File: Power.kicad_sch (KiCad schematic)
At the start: 43 parts, among them J10 Conn_01x02_Socket, J22 Conn_01x02_Socket, J23 Conn_01x02_Socket, J9 Barrel_Jack, Q1 NMOS, U10 INA219AxD, U11 TLV62569ADRL, U15 TPS60400DBV, U9 INA219AxD

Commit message: Schematic tiddy up
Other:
- title: (none) -> Power Schematic
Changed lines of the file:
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@@
 	(generator_version "10.0")
 	(paper "A4")
+	(title_block
+		(title "Power Schematic")
+		(date "2026-10-17")
+		(rev "0")
+		(comment 1 "Javier Aldana + Xander Beal")
+	)
 	(rectangle
 		(start 110.49 101.6)

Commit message: small changes
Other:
- moved on the sheet: C43, C47, C48, C49, C50, D4, J22, J23, R33, R38, R39, U15

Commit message: Final PCB from Xander
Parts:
- removed J9: Barrel_Jack, Connector_BarrelJack:BarrelJack_SwitchcraftConxall_RAPC10U_Horizontal, symbol Connector:Barrel_Jack
- added J24: Conn_01x02_Socket, Connector_Phoenix_SPT:PhoenixContact_SPT_2.5_2-H-5.0_1x02_P5.0mm_Horizontal, symbol Connector:Conn_01x02_Socket
- F1: footprint Resistor_THT:R_Axial_DIN0204_L3.6mm_D1.6mm_P5.08mm_Horizontal -> Fuse:Fuseholder_Clip-5x20mm_Keystone_3512P_Inline_P23.62x7.27mm_D1.02x2.41x1.02x1.57mm_Horizontal
- J22, J23: footprint Connector_PinSocket_2.54mm:PinSocket_1x02_P2.54mm_Vertical -> Connector_PinHeader_2.54mm:PinHeader_1x02_P2.54mm_Vertical
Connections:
- net 5V: now also J10.2 (Pin_2); no longer J10.1 (Pin_1)
- net GND: now also J24.1 (Pin_1)
- net at Q1.2 (D): now also J10.1 (Pin_1); no longer J10.2 (Pin_2)
- net at F1.1: now also J24.2 (Pin_2)
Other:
- moved on the sheet: J10

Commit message: second buck
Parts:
- added C1: 1u, Capacitor_SMD:C_0603_1608Metric, symbol Device:C
- added C2, C4: 100n, symbol Device:C
- added C3: 66u, symbol Device:C
- added C5: 470pF, symbol Device:C
- added C6: 22u, Capacitor_SMD:C_0805_2012Metric, symbol Device:C
- added L2: 1.5u, symbol Device:L
- added R1: 100k, Resistor_SMD:R_0603_1608Metric, symbol Device:R
- added R2: 1k, symbol Device:R
- added R3: 73.2k, Resistor_SMD:R_0402_1005Metric, symbol Device:R
- added R4: 10k, Resistor_SMD:R_0402_1005Metric, symbol Device:R
- added U2: TPS513885VABR, VAB0013A-MFG, symbol TPS51388:TPS513885VABR
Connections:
- net GND: now also C1.2, C2.2, C3.2, C6.2, R4.2, U2.11 (PGND), U2.3 (PGND), U2.9 (FBG)
- new net: R2.1, R3.2, R4.1, U2.7 (FB)
- new net: C4.2, L2.1
- new net: C1.1, R1.1, U2.10 (VCC), U2.5 (MODE)
- new net: R1.2, U2.4 (PG)
- new net: C4.1, U2.12 (SW), U2.13 (VBST), U2.2 (SW)
- new net: C5.1, R2.2
- new net +12V: C2.1, C3.1, U2.1 (VIN)
- new net +3V3: U2.6 (EN)
- new net +5V: C5.2, C6.1, L2.2, R3.1

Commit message: bucks
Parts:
- added C7, C8: 22, symbol Device:C
- C2, C4: footprint (none) -> Capacitor_SMD:C_0603_1608Metric
- C3: value 66u -> 22
- C5: footprint (none) -> Capacitor_SMD:C_0402_1005Metric
- L2: footprint (none) -> Inductor_SMD:IHLP5050EZER1R5M01
- R2: footprint (none) -> Resistor_SMD:R_0603_1608Metric
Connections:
- net GND: no longer C3.2
- net +12V renamed 20
- net 20: no longer C3.1
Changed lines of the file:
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@@
 			)
 		)
-		(property "Footprint" ""
+		(property "Footprint" "Capacitor_SMD:C_0603_1608Metric"
 			(at 157.1752 205.74 0)
 			(hide yes)
@@
 			)
 		)
-		(property "Value" "+12V"
+		(property "Value" "20"
 			(at 146.05 173.99 0)
 			(show_name no)
@@
 			)
 		)
-		(property "Footprint" ""
+		(property "Footprint" "Inductor_SMD:IHLP5050EZER1R5M01"
 			(at 260.35 173.99 0)
 			(hide yes)
@@
 			)
 		)
-		(property "Description" "Inductor"
+		(property "Description" "IHLP5050EZER1R5M01"
 			(at 260.35 173.99 0)
 			(hide yes)
@@
 	)
 	(symbol
+		(lib_id "Device:C")
+		(at 134.62 200.66 0)
+		(unit 1)
+		(body_style 1)
+		(exclude_from_sim no)
+		(in_bom yes)
+		(on_board yes)
+		(in_pos_files yes)
+		(dnp no)
+		(fields_autoplaced yes)
+		(property "Reference" "C3"
+			(at 138.43 199.3899 0)
+			(show_name no)
+			(do_not_autoplace no)
+			(effects
+				(font
+					(size 1.27 1.27)
+				)
+				(justify left)
+			)
+		)
+		(property "Value" "22"
+			(at 138.43 201.9299 0)
+			(show_name no)
+			(do_not_autoplace no)
+			(effects
+				(font
+					(size 1.27 1.27)
+				)
+				(justify left)
+			)
+		)
+		(property "Footprint" ""
+			(at 135.5852 204.47 0)
+			(hide yes)
+			(show_name no)
+			(do_not_autoplace no)
+			(effects
+				(font
+					(size 1.27 1.27)
+				)
+			)
+		)
+		(property "Datasheet" ""
+			(at 134.62 200.66 0)
+			(hide yes)
+			(show_name no)
+			(do_not_autoplace no)
+			(effects
+				(font
+					(size 1.27 1.27)
+				)
+			)
+		)
+		(property "Description" "CL31A226KAHNNNE"
+			(at 134.62 200.66 0)
+			(hide yes)
+			(show_name no)
+			(do_not_autoplace no)
+			(effects
+				(font
+					(size 1.27 1.27)
+				)
+			)
+		)
+		(pin "2"
+		)
+		(pin "1"
+		)
+		(instances
+			(project "Power"
+				(path "/ce54564b-053f-4184-8bbf-14aa73263a86"
+					(reference "C3")
+					(unit 1)
+				)
+			)
+		)
+	)
+	(symbol
 		(lib_id "power:+3V3")
 		(at 41.91 111.76 0)
@@
 			)
 		)
-		(property "Footprint" ""
+		(property "Footprint" "Capacitor_SMD:C_0603_1608Metric"
 			(at 248.92 173.0248 0)
 			(hide yes)
@@
 			)
 		)
-		(property "Description" "Unpolarized capacitor"
+		(property "Description" "EMK107B7104KA-T"
 			(at 245.11 173.99 0)
 			(hide yes)
@@
 			)
 		)
-		(property "Footprint" ""
+		(property "Footprint" "Capacitor_SMD:C_0402_1005Metric"
 			(at 279.4 188.2648 0)
 			(hide yes)
@@
 			)
 		)
-		(property "Description" "Unpolarized capacitor"
+		(property "Description" "GRM1555C1E471JA01D"
 			(at 275.59 189.23 0)
 			(hide yes)
@@
 	(symbol
 		(lib_id "Device:C")
-		(at 146.05 201.93 0)
+		(at 124.46 200.66 0)
 		(unit 1)
 		(body_style 1)
@@
 		(dnp no)
 		(fields_autoplaced yes)
-		(property "Reference" "C3"
-			(at 149.86 200.6599 0)
+		(property "Reference" "C7"
+			(at 128.27 199.3899 0)
 			(show_name no)
 			(do_not_autoplace no)
@@
 			)
 		)
-		(property "Value" "66u"
-			(at 149.86 203.1999 0)
+		(property "Value" "22"
+			(at 128.27 201.9299 0)
 			(show_name no)
 			(do_not_autoplace no)
@@
 		)
 		(property "Footprint" ""
-			(at 147.0152 205.74 0)
+			(at 125.4252 204.47 0)
 			(hide yes)
 			(show_name no)
@@
 			)
 		)
-		(property "Datasheet" ""
-			(at 146.05 201.93 0)
+		(property "Datasheet" "CL31A226KAHNNNE"
+			(at 124.46 200.66 0)
 			(hide yes)
 			(show_name no)
@@
 			)
 		)
-		(property "Description" "Unpolarized capacitor"
-			(at 146.05 201.93 0)
+		(property "Description" "CL31A226KAHNNNE"
+			(at 124.46 200.66 0)
 			(hide yes)
 			(show_name no)
@@
 			)
 		)
-		(pin "1"
-		)
 		(pin "2"
 		)
+		(pin "1"
+		)
 		(instances
 			(project "Power"
 				(path "/ce54564b-053f-4184-8bbf-14aa73263a86"
-					(reference "C3")
+					(reference "C7")
 					(unit 1)
 				)
@@
 	)
 	(symbol
+		(lib_id "Device:C")
+		(at 114.3 200.66 0)
+		(unit 1)
+		(body_style 1)
+		(exclude_from_sim no)
+		(in_bom yes)
+		(on_board yes)
+		(in_pos_files yes)
+		(dnp no)
+		(fields_autoplaced yes)
+		(property "Reference" "C8"
+			(at 118.11 199.3899 0)
+			(show_name no)
+			(do_not_autoplace no)
+			(effects
+				(font
+					(size 1.27 1.27)
+				)
+				(justify left)
+			)
+		)
+		(property "Value" "22"
+			(at 118.11 201.9299 0)
+			(show_name no)
+			(do_not_autoplace no)
+			(effects
+				(font
+					(size 1.27 1.27)
+				)
+				(justify left)
+			)
+		)
+		(property "Footprint" ""
+			(at 115.2652 204.47 0)
+			(hide yes)
+			(show_name no)
+			(do_not_autoplace no)
+			(effects
+				(font
+					(size 1.27 1.27)
+				)
+			)
+		)
+		(property "Datasheet" ""
+			(at 114.3 200.66 0)
+			(hide yes)
+			(show_name no)
+			(do_not_autoplace no)
+			(effects
+				(font
+					(size 1.27 1.27)
+				)
+			)
+		)
+		(property "Description" "CL31A226KAHNNNE"
+			(at 114.3 200.66 0)
+			(hide yes)
+			(show_name no)
+			(do_not_autoplace no)
+			(effects
+				(font
+					(size 1.27 1.27)
+				)
+			)
+		)
+		(pin "2"
+		)
+		(pin "1"
+		)
+		(instances
+			(project "Power"
+				(path "/ce54564b-053f-4184-8bbf-14aa73263a86"
+					(reference "C8")
+					(unit 1)
+				)
+			)
+		)
+	)
+	(symbol
 		(lib_id "Connector:Conn_01x02_Socket")
 		(at 24.13 29.21 0)
@@
 			)
 		)
-		(property "Footprint" ""
+		(property "Footprint" "Resistor_SMD:R_0603_1608Metric"
 			(at 252.73 191.008 90)
 			(hide yes)
@@
 			)
 		)
-		(property "Description" "Resistor"
+		(property "Description" "EMK107B7104KA-T"
 			(at 252.73 189.23 0)
 			(hide yes)

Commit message: fixing some ERC issues
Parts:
- C3, C7, C8: footprint (none) -> Capacitor_SMD:C_1210_3225Metric
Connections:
- net 20: now also C3.1, C7.1, C8.1
- net GND: now also C3.2, C7.2, C8.2
- net at C4.2, L2.1: now also U2.12 (SW), U2.2 (SW)
- net at C4.1, U2.13 (VBST): no longer U2.12 (SW), U2.2 (SW)
- no-connect marks 0 -> 1
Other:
- moved on the sheet: C3, C7, C8

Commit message: footprintfor buck
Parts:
- removed C4: 100n, Capacitor_SMD:C_0603_1608Metric, symbol Device:C
- removed C5: 470pF, Capacitor_SMD:C_0402_1005Metric, symbol Device:C
- removed C6: 22u, Capacitor_SMD:C_0805_2012Metric, symbol Device:C
- removed R2: 1k, Resistor_SMD:R_0603_1608Metric, symbol Device:R
- removed R3: 73.2k, Resistor_SMD:R_0402_1005Metric, symbol Device:R
- removed U2: TPS513885VABR, VAB0013A-MFG, symbol TPS51388:TPS513885VABR
- added C30: 100n, Capacitor_SMD:C_0603_1608Metric, symbol Device:C
- added C31: 470pF, Capacitor_SMD:C_0402_1005Metric, symbol Device:C
- added C56: 22u, Capacitor_SMD:C_0805_2012Metric, symbol Device:C
- added J9: Conn_01x02_Pin, Connector_PinHeader_2.54mm:PinHeader_1x02_P2.54mm_Vertical, symbol Connector:Conn_01x02_Pin
- added R16: 1k, Resistor_SMD:R_0603_1608Metric, symbol Device:R
- added R63: 73.2k, Resistor_SMD:R_0402_1005Metric, symbol Device:R
- added U4: TPS513885VABR, TPS513885VABR:VAB0013A-MFG, symbol TPS51388:TPS513885VABR
- renumbered C8 to C61, C7 to C62, C3 to C63, C2 to C64, C1 to C65, L2 to L10
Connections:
- net +3V3: now also U4.6 (EN)
- net +5V: now also C31.2, C56.1, R63.1
- net GND: now also C56.2, J9.2 (Pin_2), U4.11 (PGND), U4.3 (PGND), U4.9 (FBG)
- net at R4.1: now also R16.1, R63.2, U4.7 (FB)
- net at L10.1: now also C30.2, U4.12 (SW), U4.2 (SW)
- net at C65.1, R1.1: now also U4.10 (VCC), U4.5 (MODE)
- net at R1.2: now also U4.4 (PG)
- net 20 renamed +20V
- net +20V: now also J9.1 (Pin_1), U4.1 (VIN)
- new net: C30.1, U4.13 (VBST)
- new net: C31.1, R16.2

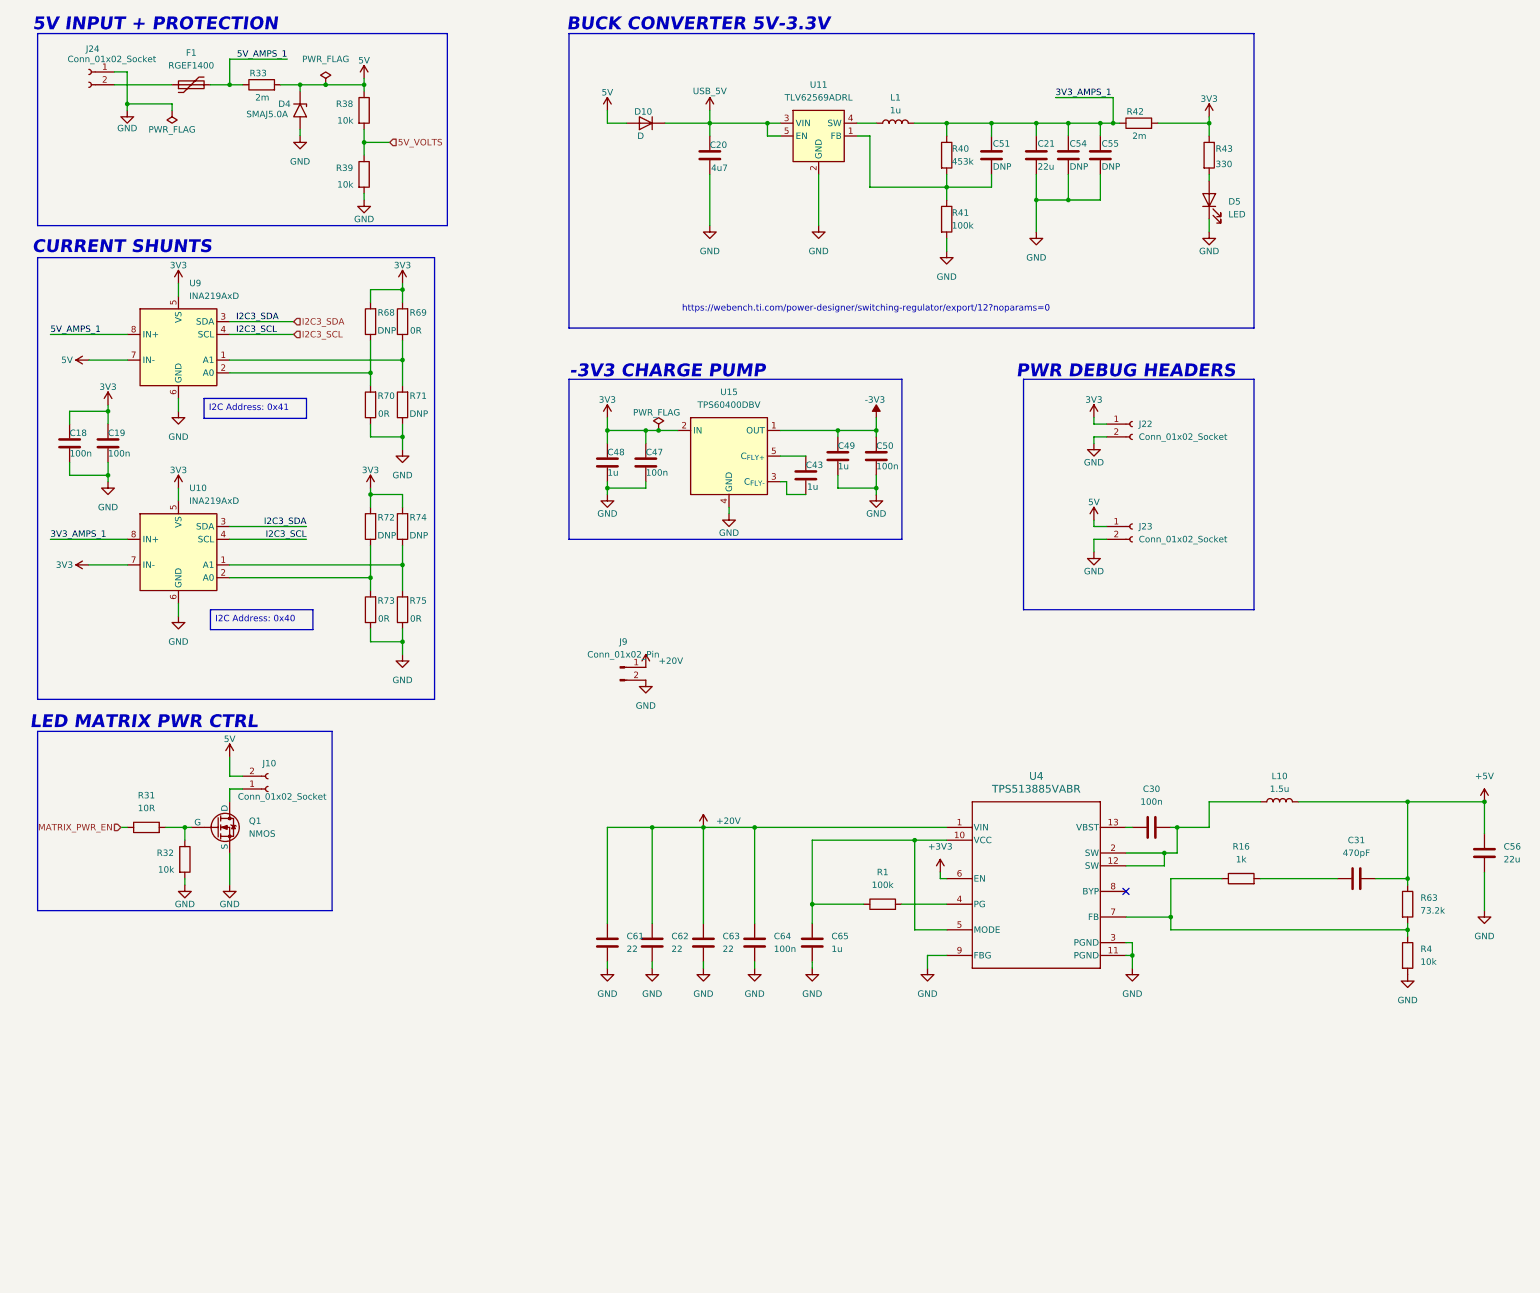
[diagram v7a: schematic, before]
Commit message: moving usbc to power section, added poewr delivery IC
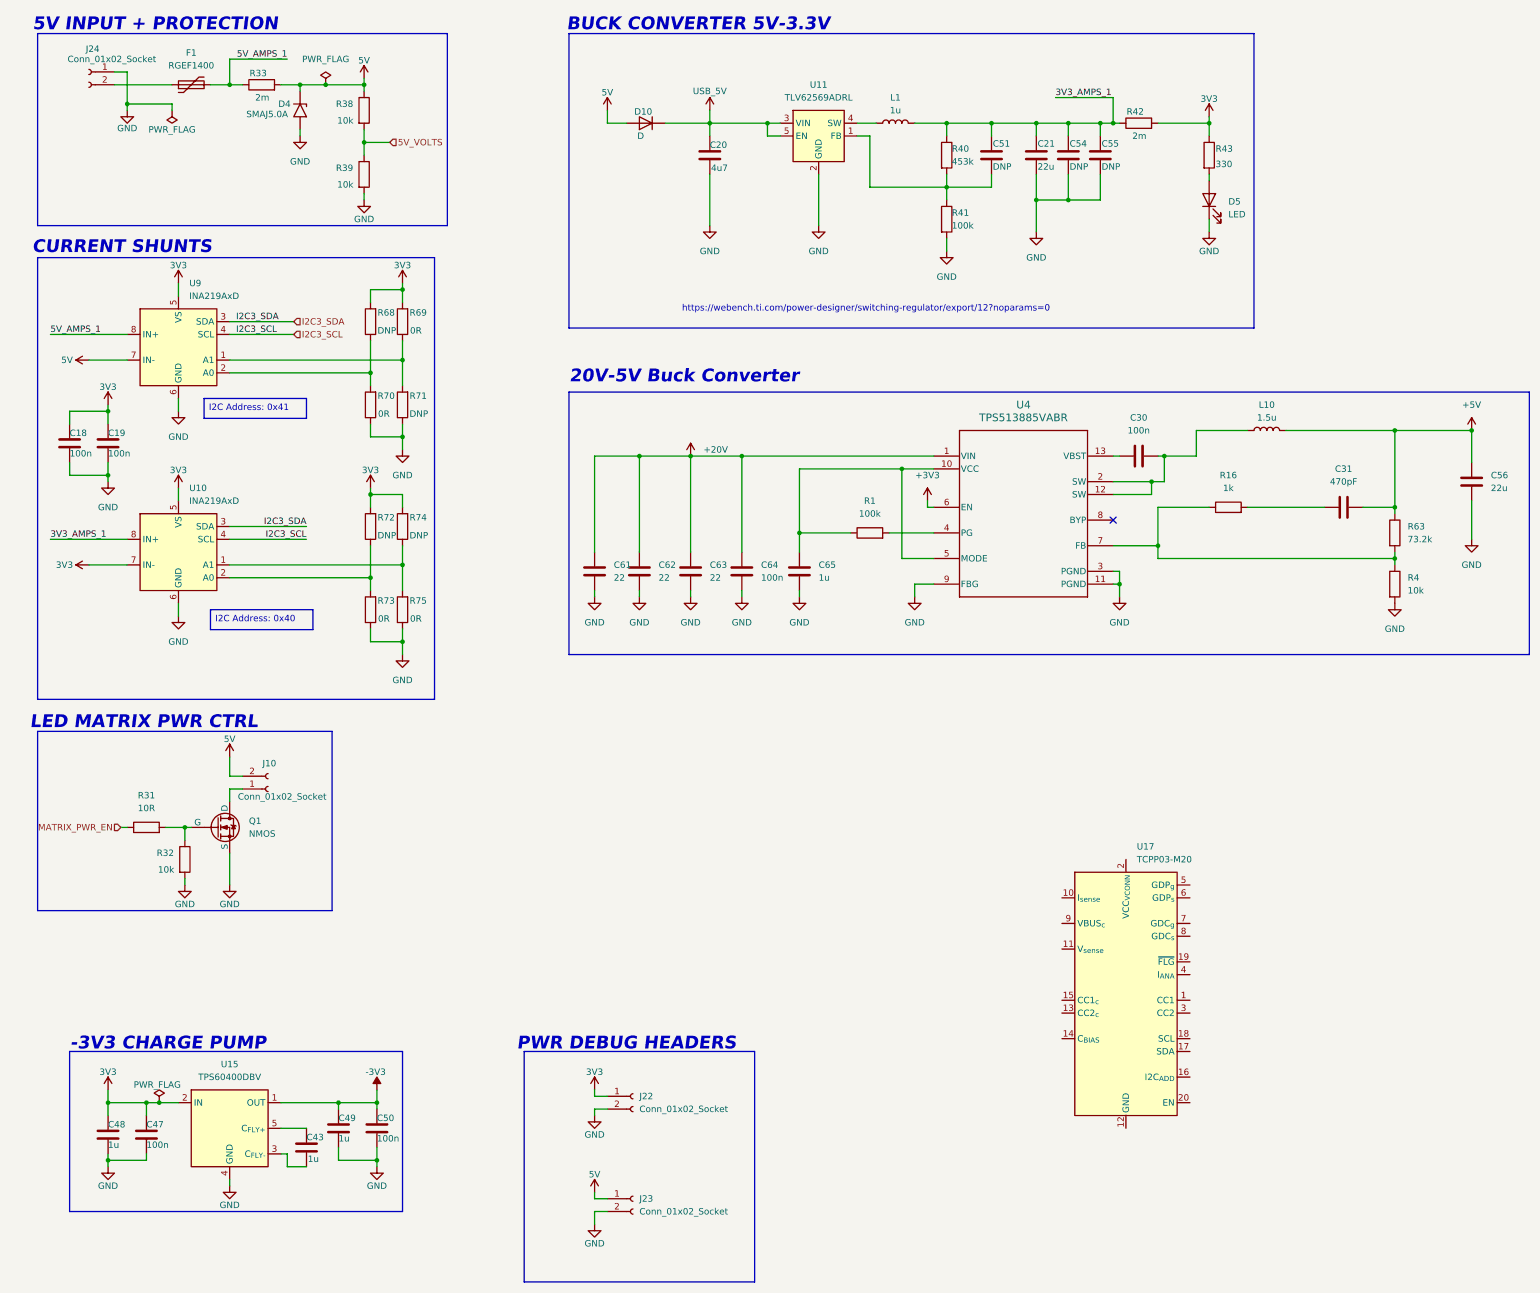
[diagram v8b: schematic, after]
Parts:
- removed J9: Conn_01x02_Pin, Connector_PinHeader_2.54mm:PinHeader_1x02_P2.54mm_Vertical, symbol Connector:Conn_01x02_Pin
- added U17: TCPP03-M20, Package_DFN_QFN:TQFN-20-1EP_4x4mm_P0.5mm_EP2.1x2.1mm, symbol Interface_USB:TCPP03-M20
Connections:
- new net: U17.12 (GND), U17.21 (GND)
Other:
- note added: "20V-5V Buck Converter"
- moved on the sheet: C30, C31, C43, C47, C48, C49, C50, C56, C61, C62, C63, C64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
